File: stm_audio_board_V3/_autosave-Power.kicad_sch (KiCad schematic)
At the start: 38 parts, among them J5 Barrel_Jack_MountingPin, U1 IS42S16100H-7TL, U2 OP275, U3 MP-K7805-500R3, U4 OP275, U5 MIC2920A-3.3WS-TR, U6 L7809, U9 MIC2920A-3.3WS-TR

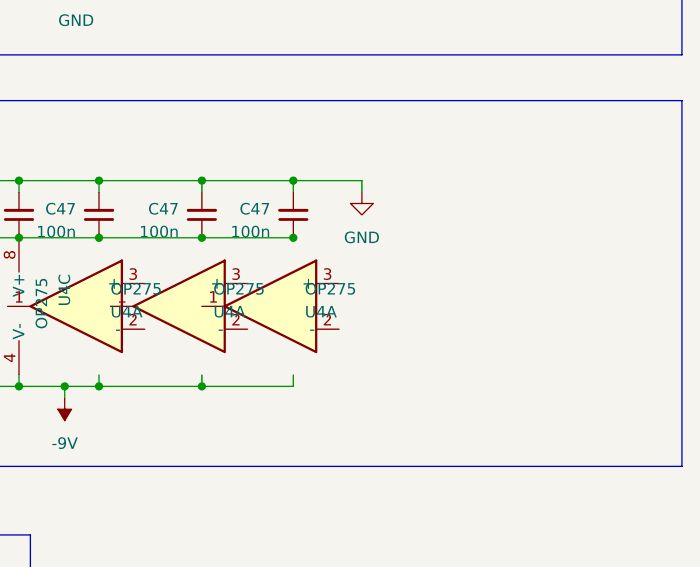
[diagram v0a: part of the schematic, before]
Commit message: Input output connected to codec
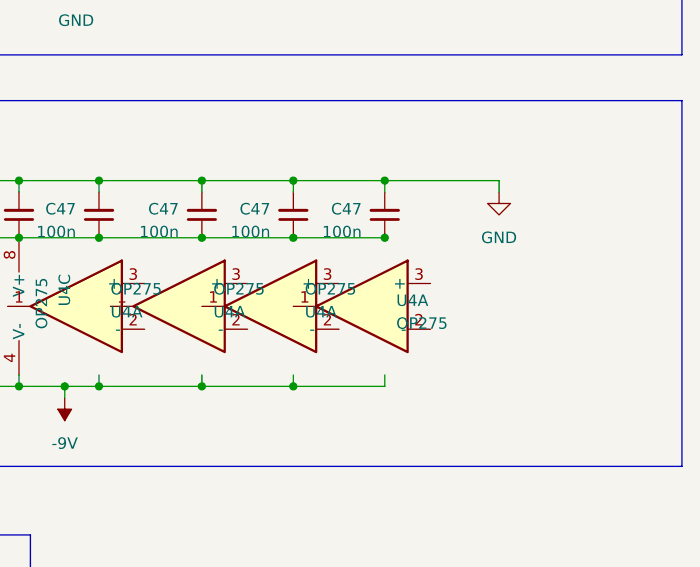
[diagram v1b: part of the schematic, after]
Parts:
- added C47: 100n, Capacitor_SMD:C_0603_1608Metric, symbol Device:C_Small
- added U4: OP275, Package_SO:SSOP-8_3.9x5.05mm_P1.27mm, symbol Amplifier_Operational:OP275
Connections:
- net +9V: now also C47.1
- net GND: now also C47.2
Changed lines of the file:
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@@
   (junction (at 90.17 91.44) (diameter 0) (color 0 0 0 0)
   )
+  (junction (at 270.51 81.28) (diameter 0) (color 0 0 0 0)
+  )
   (junction (at 201.93 208.28) (diameter 0) (color 0 0 0 0)
   )
   (junction (at 201.93 215.9) (diameter 0) (color 0 0 0 0)
   )
+  (junction (at 270.51 87.63) (diameter 0) (color 0 0 0 0)
+  )
   (junction (at 250.19 87.63) (diameter 0) (color 0 0 0 0)
   )
@@
   (junction (at 168.91 189.23) (diameter 0) (color 0 0 0 0)
   )
+  (junction (at 260.35 104.14) (diameter 0) (color 0 0 0 0)
+  )
   (junction (at 201.93 210.82) (diameter 0) (color 0 0 0 0)
   )
@@
     (stroke (width 0) (type default))
   )
-  (wire (pts (xy 267.97 81.28) (xy 267.97 82.55))
+  (wire (pts (xy 283.21 81.28) (xy 283.21 82.55))
     (stroke (width 0) (type default))
   )
@@
     (stroke (width 0) (type default))
   )
+  (wire (pts (xy 270.51 81.28) (xy 270.51 82.55))
+    (stroke (width 0) (type default))
+  )
   (wire (pts (xy 90.17 91.44) (xy 113.03 91.44))
     (stroke (width 0) (type default))
@@
     (stroke (width 0) (type default))
   )
+  (wire (pts (xy 260.35 104.14) (xy 270.51 104.14))
+    (stroke (width 0) (type default))
+  )
   (wire (pts (xy 140.97 138.43) (xy 140.97 140.97))
     (stroke (width 0) (type default))
@@
     (stroke (width 0) (type default))
   )
+  (wire (pts (xy 270.51 102.87) (xy 270.51 104.14))
+    (stroke (width 0) (type default))
+  )
   (wire (pts (xy 238.76 87.63) (xy 250.19 87.63))
     (stroke (width 0) (type default))
@@
     (stroke (width 0) (type default))
   )
+  (wire (pts (xy 260.35 87.63) (xy 270.51 87.63))
+    (stroke (width 0) (type default))
+  )
   (wire (pts (xy 203.2 194.31) (xy 203.2 196.85))
     (stroke (width 0) (type default))
@@
     (stroke (width 0) (type default))
   )
+  (wire (pts (xy 270.51 81.28) (xy 283.21 81.28))
+    (stroke (width 0) (type default))
+  )
   (wire (pts (xy 153.67 138.43) (xy 165.1 138.43))
     (stroke (width 0) (type default))
@@
     (stroke (width 0) (type default))
   )
-  (wire (pts (xy 260.35 81.28) (xy 267.97 81.28))
+  (wire (pts (xy 260.35 81.28) (xy 270.51 81.28))
     (stroke (width 0) (type default))
   )
@@
     )
   )
+  (symbol (lib_id "Amplifier_Operational:OP275") (at 267.97 95.25 0) (mirror y) (unit 1)
+    (in_bom yes) (on_board yes) (dnp no) (fields_autoplaced)
+    (property "Reference" "U4" (at 271.78 94.615 0)
+      (effects (font (size 1.27 1.27)) (justify right))
+    )
+    (property "Value" "OP275" (at 271.78 97.155 0)
+      (effects (font (size 1.27 1.27)) (justify right))
+    )
+    (property "Footprint" "Package_SO:SSOP-8_3.9x5.05mm_P1.27mm" (at 267.97 95.25 0)
+      (effects (font (size 1.27 1.27)) hide)
+    )
+    (property "Datasheet" "https://www.analog.com/media/en/technical-documentation/data-sheets/OP275.pdf" (at 267.97 95.25 0)
+      (effects (font (size 1.27 1.27)) hide)
+    )
+    (property "JLCPCB" "C161797" (at 267.97 95.25 0)
+      (effects (font (size 1.27 1.27)) hide)
+    )
+    (property "Field5" "" (at 267.97 95.25 0)
+      (effects (font (size 1.27 1.27)) hide)
+    )
+    (pin "1")
+    (pin "2")
+    (pin "3")
+    (pin "5")
+    (pin "6")
+    (pin "7")
+    (pin "4")
+    (pin "8")
+    (instances
+      (project "stm_audio_board_V3"
+        (path "/6997cf63-2615-4e49-9471-e7da1b6bae71"
+          (reference "U4") (unit 1)
+        )
+        (path "/6997cf63-2615-4e49-9471-e7da1b6bae71/f20dc640-ad21-4977-8df1-611625087c69"
+          (reference "U10") (unit 3)
+        )
+        (path "/6997cf63-2615-4e49-9471-e7da1b6bae71/2eb2ee8f-ab98-4666-97f0-bfacb073bc88"
+          (reference "U14") (unit 3)
+        )
+      )
+    )
+  )
   (symbol (lib_id "power:GND") (at 34.29 49.53 0) (unit 1)
     (in_bom yes) (on_board yes) (dnp no) (fields_autoplaced)
@@
     )
   )
+  (symbol (lib_id "Device:C_Small") (at 270.51 85.09 0) (mirror x) (unit 1)
+    (in_bom yes) (on_board yes) (dnp no) (fields_autoplaced)
+    (property "Reference" "C47" (at 267.97 84.4486 0)
+      (effects (font (size 1.27 1.27)) (justify right))
+    )
+    (property "Value" "100n" (at 267.97 86.9886 0)
+      (effects (font (size 1.27 1.27)) (justify right))
+    )
+    (property "Footprint" "Capacitor_SMD:C_0603_1608Metric" (at 270.51 85.09 0)
+      (effects (font (size 1.27 1.27)) hide)
+    )
+    (property "Datasheet" "~" (at 270.51 85.09 0)
+      (effects (font (size 1.27 1.27)) hide)
+    )
+    (pin "1")
+    (pin "2")
+    (instances
+      (project "stm_audio_board_V3"
+        (path "/6997cf63-2615-4e49-9471-e7da1b6bae71"
+          (reference "C47") (unit 1)
+        )
+        (path "/6997cf63-2615-4e49-9471-e7da1b6bae71/83920463-7bb1-4088-aad8-702bcdea14ea"
+          (reference "C63") (unit 1)
+        )
+        (path "/6997cf63-2615-4e49-9471-e7da1b6bae71/8744407a-1e34-4228-b7c6-9fdc39f322d4"
+          (reference "C25") (unit 1)
+        )
+        (path "/6997cf63-2615-4e49-9471-e7da1b6bae71/2eb2ee8f-ab98-4666-97f0-bfacb073bc88"
+          (reference "C121") (unit 1)
+        )
+      )
+    )
+  )
   (symbol (lib_id "Device:C_Polarized_Small_US") (at 49.53 46.99 0) (unit 1)
     (in_bom yes) (on_board yes) (dnp no) (fields_autoplaced)
@@
     )
   )
-  (symbol (lib_id "power:GND") (at 267.97 82.55 0) (unit 1)
-    (in_bom yes) (on_board yes) (dnp no) (fields_autoplaced)
-    (property "Reference" "#PWR03" (at 267.97 88.9 0)
-      (effects (font (size 1.27 1.27)) hide)
-    )
-    (property "Value" "GND" (at 267.97 87.63 0)
-      (effects (font (size 1.27 1.27)))
-    )
-    (property "Footprint" "" (at 267.97 82.55 0)
-      (effects (font (size 1.27 1.27)) hide)
-    )
-    (property "Datasheet" "" (at 267.97 82.55 0)
-      (effects (font (size 1.27 1.27)) hide)
-    )
+  (symbol (lib_id "power:GND") (at 283.21 82.55 0) (unit 1)
+    (in_bom yes) (on_board yes) (dnp no) (fields_autoplaced)
+    (property "Reference" "#PWR03" (at 283.21 88.9 0)
+      (effects (font (size 1.27 1.27)) hide)
+    )
+    (property "Value" "GND" (at 283.21 87.63 0)
+      (effects (font (size 1.27 1.27)))
+    )
+    (property "Footprint" "" (at 283.21 82.55 0)
+      (effects (font (size 1.27 1.27)) hide)
+    )
+    (property "Datasheet" "" (at 283.21 82.55 0)
+      (effects (font (size 1.27 1.27)) hide)
+    )
